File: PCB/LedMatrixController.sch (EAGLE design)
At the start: 9 parts, among them IC1 AT90S2313S, IC2 74LS595D

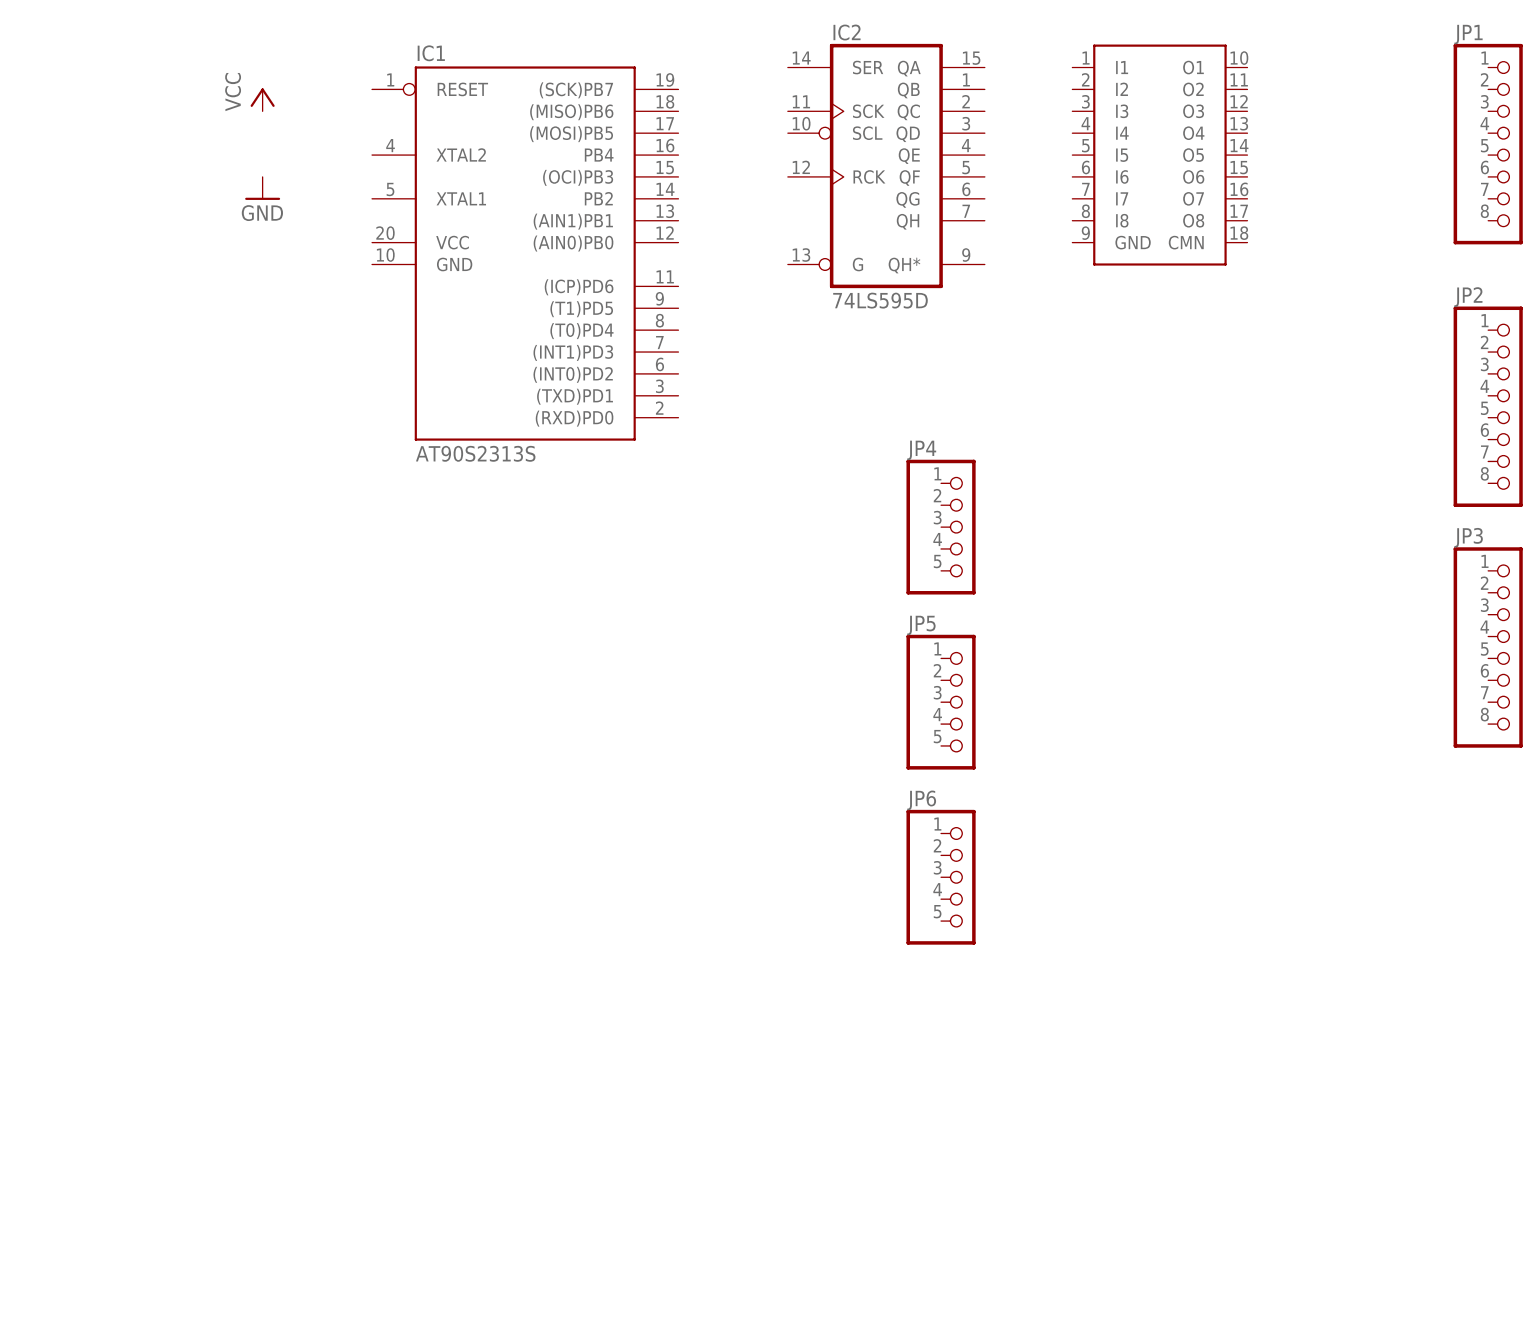
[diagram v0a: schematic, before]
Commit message: Added connections between main elements. Created dimensions on the pbc layout.
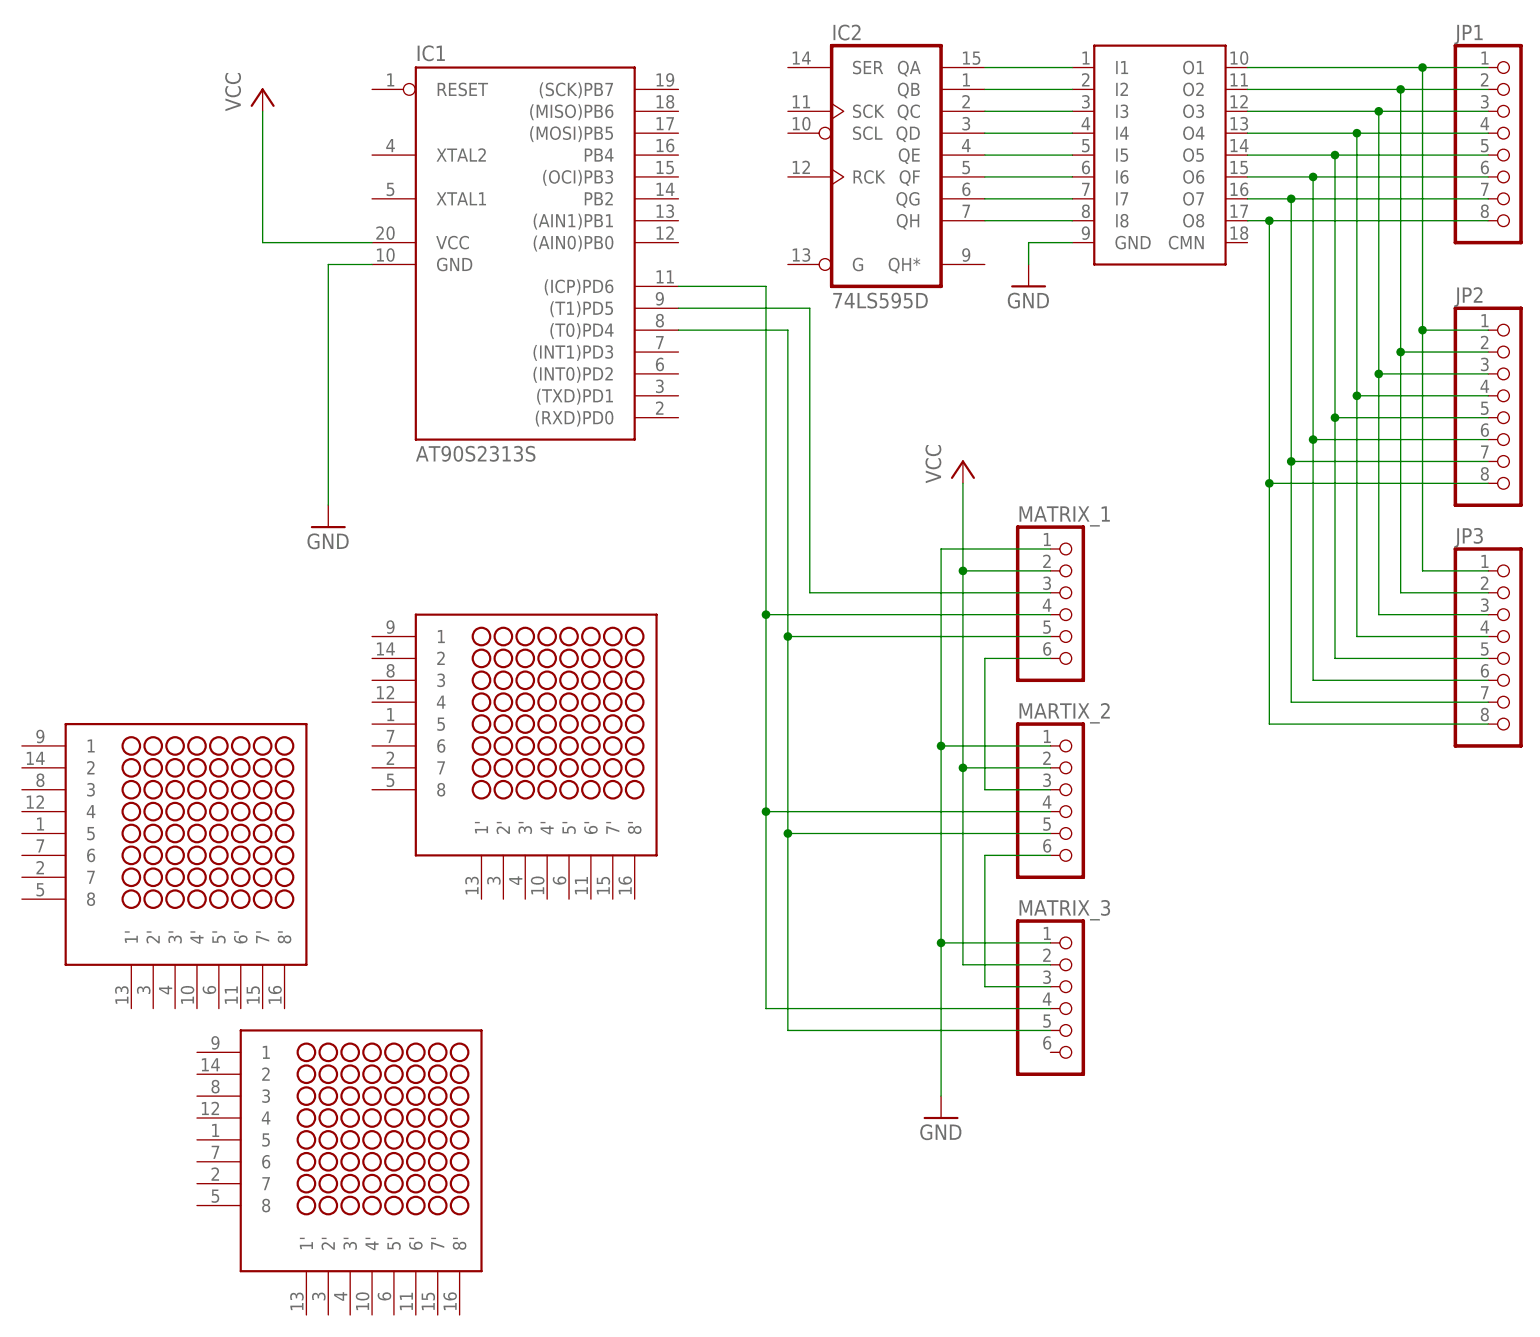
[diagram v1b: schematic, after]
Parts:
- removed JP4, JP5, JP6: (no value), pinhead:PINHD-1X5
- added MARTIX_2, MATRIX_1, MATRIX_3: (no value), pinhead:PINHD-1X6
- added U$2, U$3, U$4: NFM-12881BG-11, led_matrix_8x8:NFM-12881BG-11
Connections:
- new net CLK: IC1.(ICP)PD6, MARTIX_2.4, MATRIX_1.4, MATRIX_3.4
- new net GND: IC1.GND, MARTIX_2.1, MATRIX_1.1, MATRIX_3.1, U$1.GND
- new net N$10: MARTIX_2.3, MATRIX_1.6
- new net N$11: MARTIX_2.6, MATRIX_3.3
- new net N$12: IC1.(T1)PD5, MATRIX_1.3
- new net N$9: IC1.(T0)PD4, MARTIX_2.5, MATRIX_1.5, MATRIX_3.5
- new net R1: IC2A.QA, U$1.I1
- new net R2: IC2A.QB, U$1.I2
- new net R3: IC2A.QC, U$1.I3
- new net R4: IC2A.QD, U$1.I4
- new net R5: IC2A.QE, U$1.I5
- new net R6: IC2A.QF, U$1.I6
- new net R7: IC2A.QG, U$1.I7
- new net R8: IC2A.QH, U$1.I8
- new net ROW1: JP1.1, JP2.1, JP3.1, U$1.O1
- new net ROW2: JP1.2, JP2.2, JP3.2, U$1.O2
- new net ROW3: JP1.3, JP2.3, JP3.3, U$1.O3
- new net ROW4: JP1.4, JP2.4, JP3.4, U$1.O4
- new net ROW5: JP1.5, JP2.5, JP3.5, U$1.O5
- new net ROW6: JP1.6, JP2.6, JP3.6, U$1.O6
- new net ROW7: JP1.7, JP2.7, JP3.7, U$1.O7
- new net ROW8: JP1.8, JP2.8, JP3.8, U$1.O8
- new net VCC: IC1.VCC, MARTIX_2.2, MATRIX_1.2, MATRIX_3.2

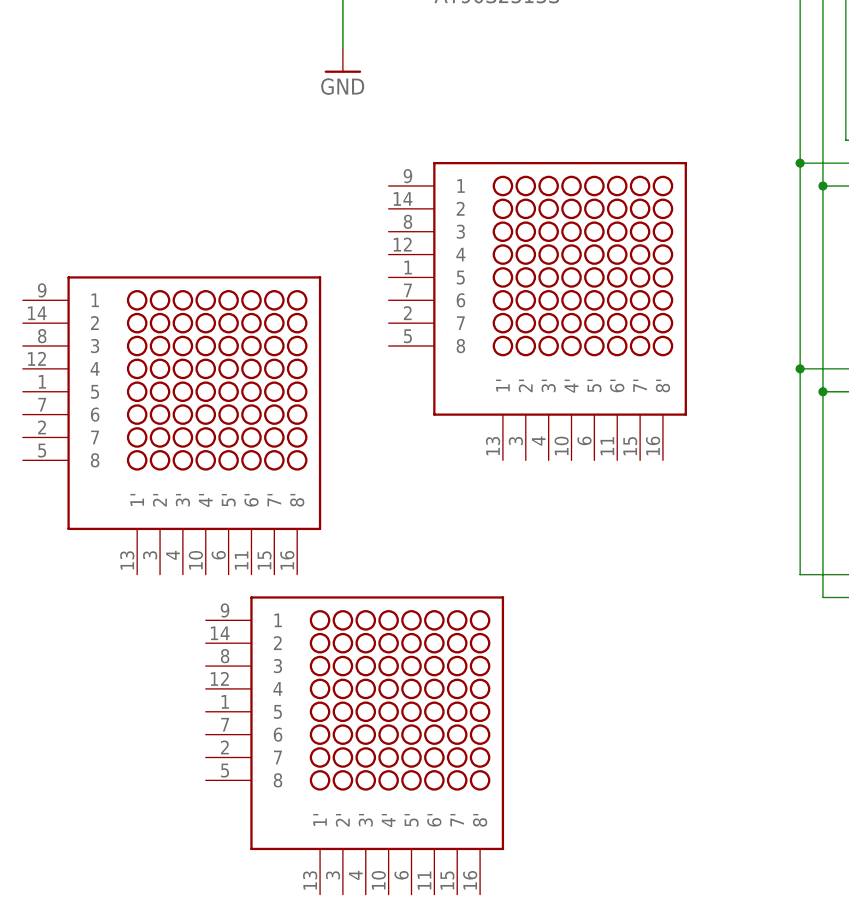
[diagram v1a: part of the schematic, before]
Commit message: Corrected positions of pinheads on the matrix controller board.
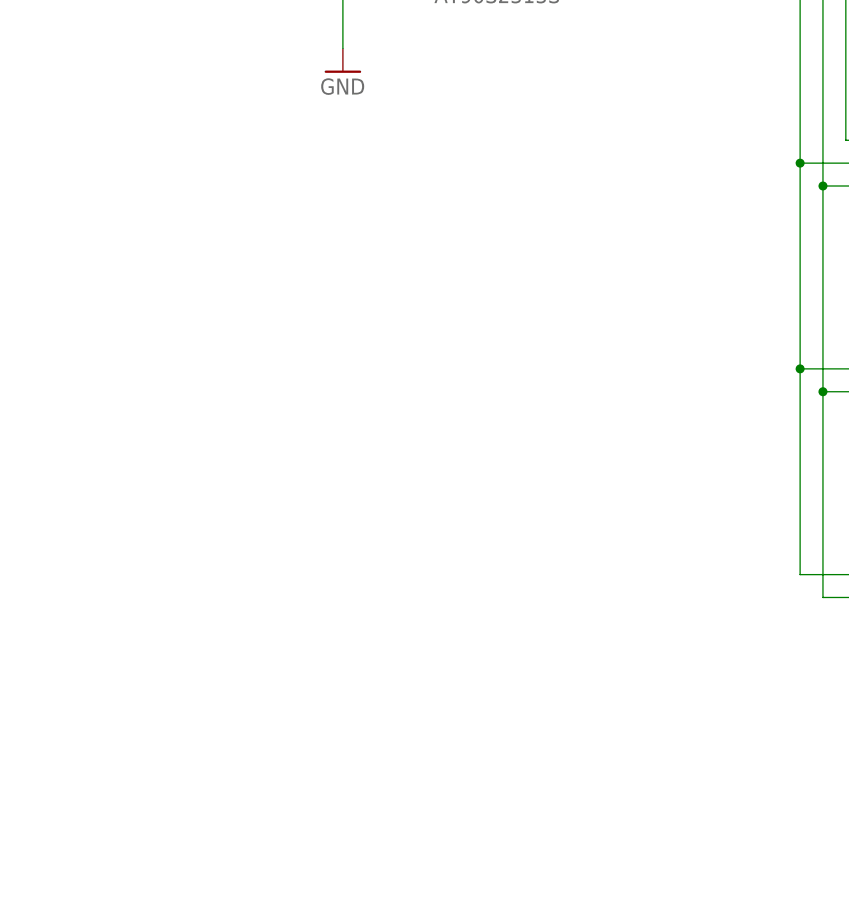
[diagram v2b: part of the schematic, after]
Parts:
- removed U$2, U$3, U$4: NFM-12881BG-11, led_matrix_8x8:NFM-12881BG-11
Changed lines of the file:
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@@
 <part name="P+2" library="supply1" deviceset="VCC" device=""/>
 <part name="GND3" library="supply1" deviceset="GND" device=""/>
-<part name="U$2" library="led_matrix_8x8" deviceset="NFM-12881BG-11" device=""/>
-<part name="U$3" library="led_matrix_8x8" deviceset="NFM-12881BG-11" device=""/>
-<part name="U$4" library="led_matrix_8x8" deviceset="NFM-12881BG-11" device=""/>
 </parts>
 <sheets>
@@
 <instance part="P+2" gate="VCC" x="96.52" y="20.32"/>
 <instance part="GND3" gate="1" x="93.98" y="-55.88"/>
-<instance part="U$2" gate="G$1" x="48.26" y="-10.16"/>
-<instance part="U$3" gate="G$1" x="7.62" y="-22.86"/>
-<instance part="U$4" gate="G$1" x="27.94" y="-58.42"/>
 </instances>
 <busses>

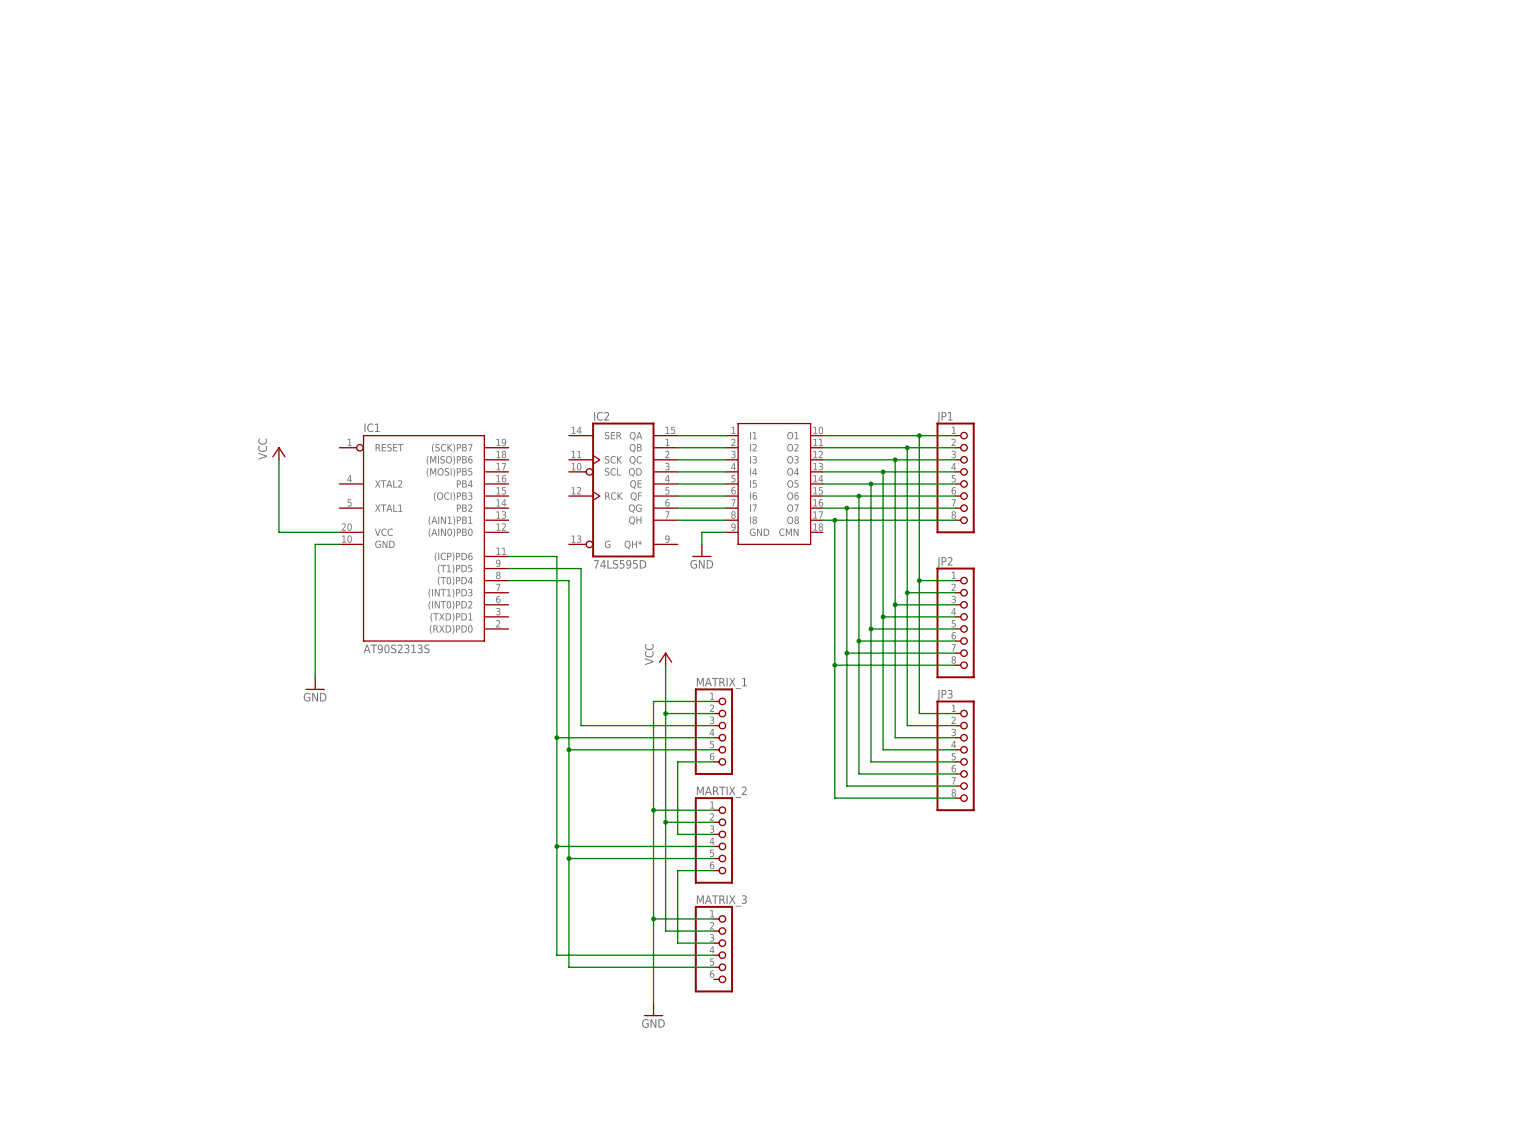
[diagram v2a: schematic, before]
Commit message: Another part of improvements in pcb layouts. Especially in pinhead area, to match both pcbs.
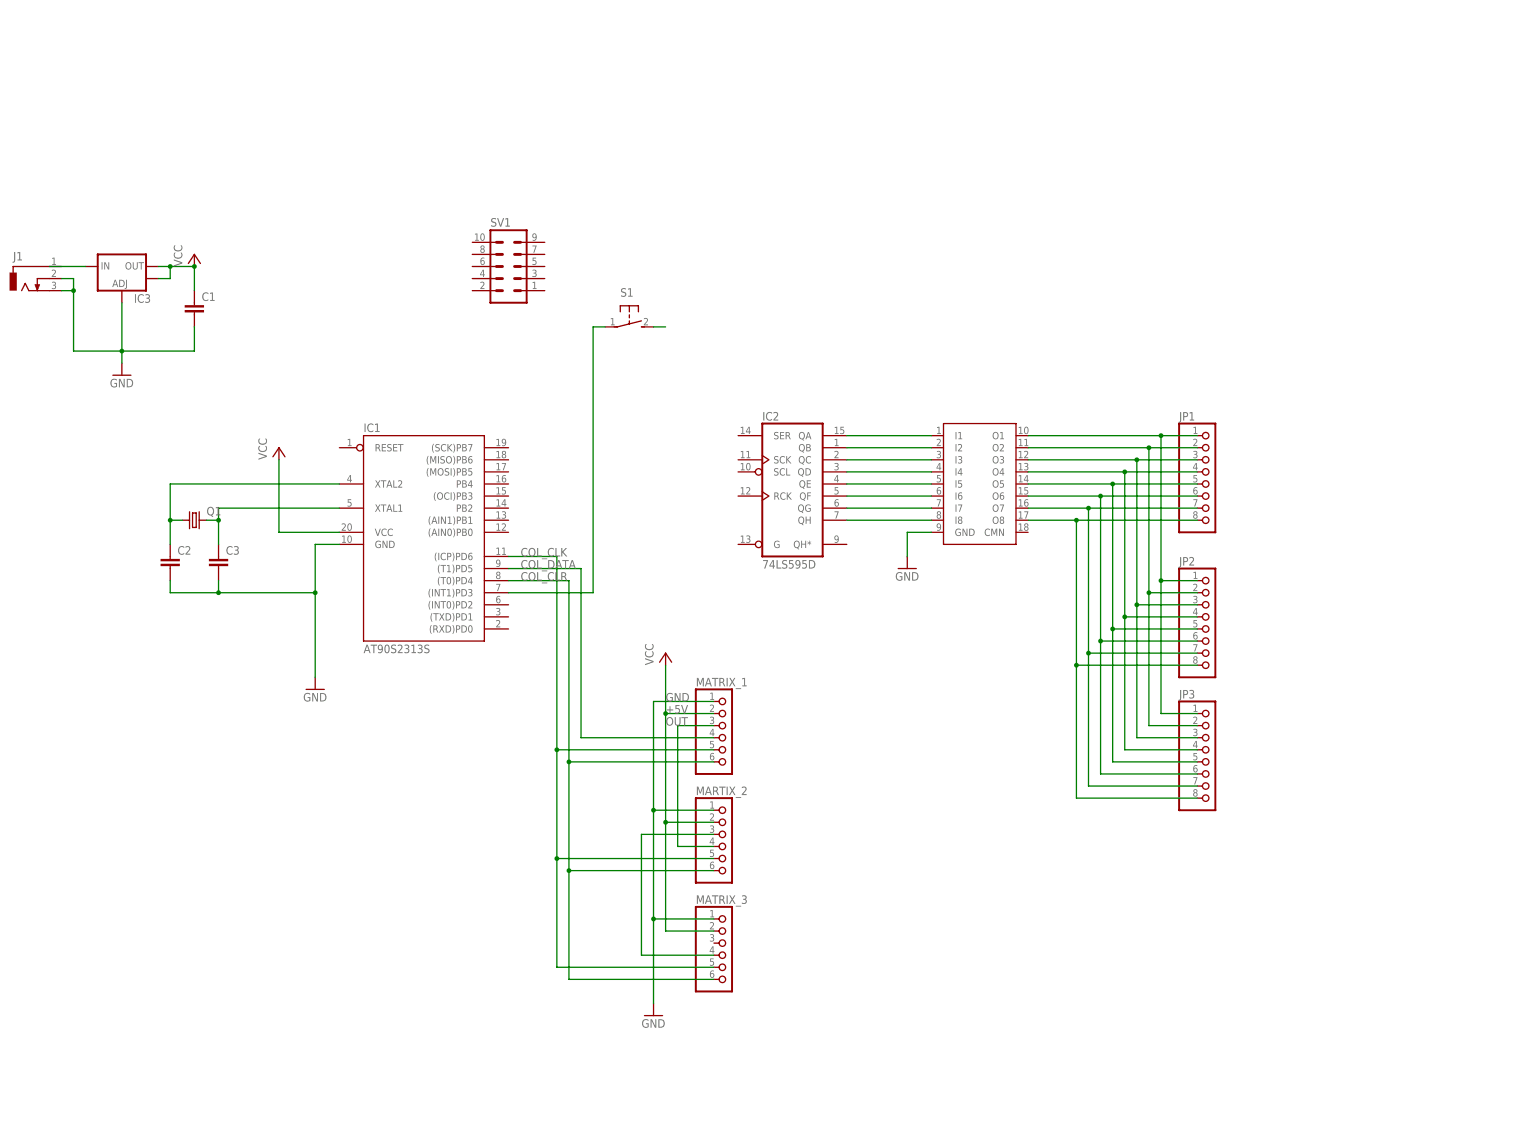
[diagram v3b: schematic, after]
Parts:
- added C1: (no value), resistor:C-EU025-025X050
- added C2, C3: (no value), resistor:C-EUC1206
- added IC3: (no value), SparkFun-PowerIC:V_REG_LM1117SOT223
- added J1: (no value), con-jack:DCJ0303
- added Q1: (no value), crystal:CRYSTALHC49UP
- added S1: (no value), switch-omron:31-XX
- added SV1: (no value), con-ml:ML10
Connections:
- removed net CLK: IC1.(ICP)PD6, MARTIX_2.4, MATRIX_1.4, MATRIX_3.4
- removed net N$10: MARTIX_2.3, MATRIX_1.6
- removed net N$11: MARTIX_2.6, MATRIX_3.3
- removed net N$12: IC1.(T1)PD5, MATRIX_1.3
- removed net N$9: IC1.(T0)PD4, MARTIX_2.5, MATRIX_1.5, MATRIX_3.5
- removed net VCC: IC1.VCC, MARTIX_2.2, MATRIX_1.2, MATRIX_3.2
- new net +5V: C1.1, IC1.VCC, IC3.OUT, IC3.OUT@1, MARTIX_2.2, MATRIX_1.2, MATRIX_3.2
- new net COL_CLK: IC1.(ICP)PD6, MARTIX_2.5, MATRIX_1.5, MATRIX_3.5
- new net COL_CLR: IC1.(T0)PD4, MARTIX_2.6, MATRIX_1.6, MATRIX_3.6
- new net COL_DATA: IC1.(T1)PD5, MATRIX_1.4
- new net N$1: C2.1, IC1.XTAL2, Q1.1
- new net N$2: IC3.IN, J1.1
- new net N$3: C3.1, IC1.XTAL1, Q1.2
- new net N$4: IC1.(INT1)PD3, S1.P
- new net N$5: S1.S
- new net N$8: MARTIX_2.3, MATRIX_3.4
- new net OUT: MARTIX_2.4, MATRIX_1.3
- net GND: now also C1.2, C2.2, C3.2, IC3.ADJ, J1.2, J1.3
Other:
- moved on the sheet: IC2, JP1, JP2, JP3
